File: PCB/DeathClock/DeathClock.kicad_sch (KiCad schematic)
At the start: 1 part

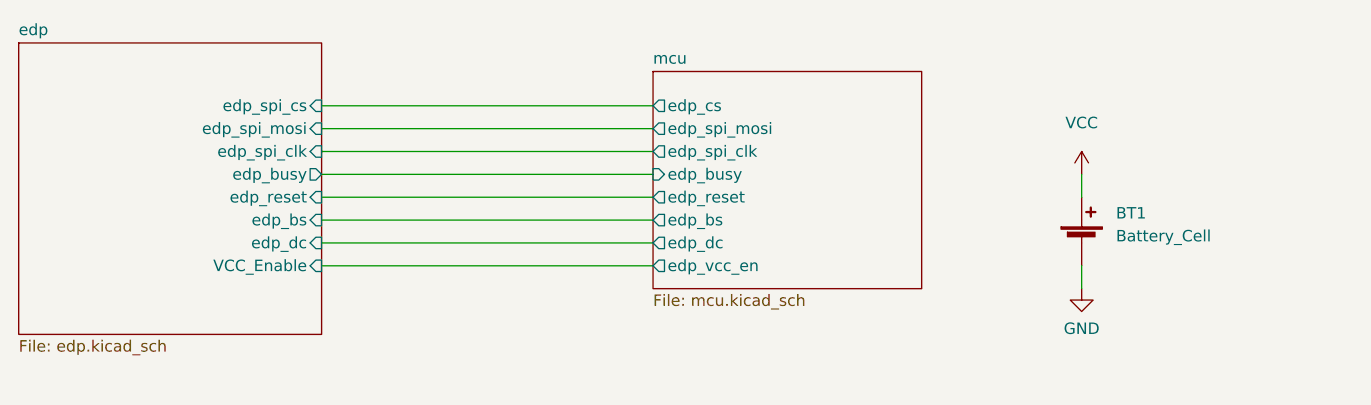
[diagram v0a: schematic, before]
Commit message: made the coin cell symbol 4 pins to make drc happy
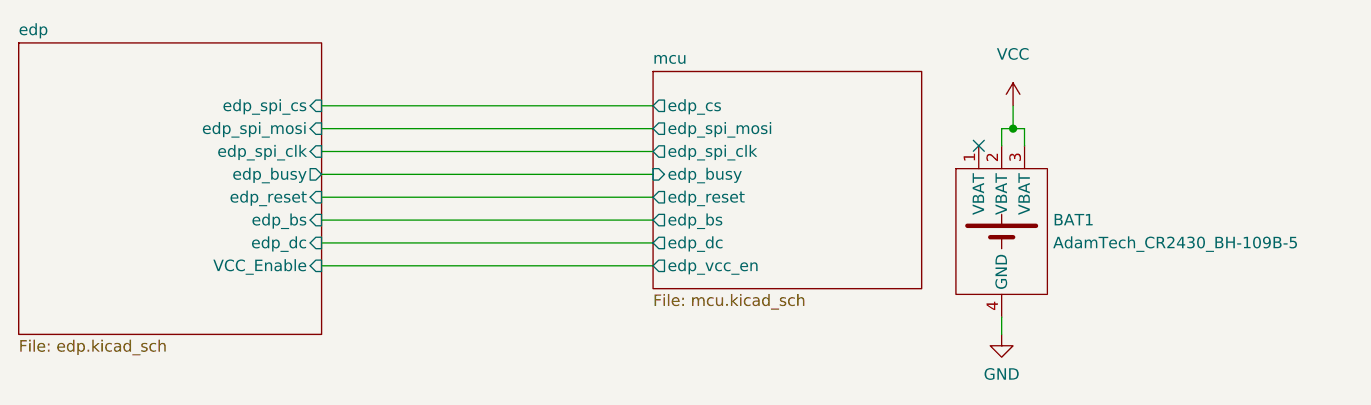
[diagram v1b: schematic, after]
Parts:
- removed BT1: Battery_Cell, CoinCellHolder:AdamTech_CR2430_BH-109B-5, symbol Device:Battery_Cell
- added BAT1: AdamTech_CR2430_BH-109B-5, CoinCellHolder:AdamTech_CR2430_BH-109B-5_num_pads, symbol CoinCellHolder:AdamTech_CR2430_BH-109B-5
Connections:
- net GND: now also BAT1.4 (GND)
- net VCC: now also BAT1.2 (VBAT), BAT1.3 (VBAT)
- no-connect marks 0 -> 1
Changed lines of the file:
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@@
 (kicad_sch (version 20211123) (generator eeschema)
   (paper "A4")
+  (junction (at 216.535 50.8) (diameter 0) (color 0 0 0 0)
+  )
+  (no_connect (at 212.725 52.705))
+  (wire (pts (xy 215.265 71.755) (xy 215.265 73.66))
+    (stroke (width 0) (type default) (color 0 0 0 0))
+  )
   (wire (pts (xy 139.7 55.88) (xy 176.53 55.88))
     (stroke (width 0) (type default) (color 0 0 0 0))
@@
     (stroke (width 0) (type default) (color 0 0 0 0))
   )
+  (wire (pts (xy 216.535 50.8) (xy 215.265 50.8))
+    (stroke (width 0) (type default) (color 0 0 0 0))
+  )
+  (wire (pts (xy 217.805 50.8) (xy 216.535 50.8))
+    (stroke (width 0) (type default) (color 0 0 0 0))
+  )
   (wire (pts (xy 139.7 58.42) (xy 176.53 58.42))
     (stroke (width 0) (type default) (color 0 0 0 0))
   )
-  (wire (pts (xy 224.155 55.88) (xy 224.155 58.42))
-    (stroke (width 0) (type default) (color 0 0 0 0))
-  )
   (wire (pts (xy 139.7 48.26) (xy 176.53 48.26))
     (stroke (width 0) (type default) (color 0 0 0 0))
   )
-  (wire (pts (xy 224.155 66.04) (xy 224.155 68.58))
+  (wire (pts (xy 216.535 48.26) (xy 216.535 50.8))
+    (stroke (width 0) (type default) (color 0 0 0 0))
+  )
+  (wire (pts (xy 215.265 50.8) (xy 215.265 52.705))
     (stroke (width 0) (type default) (color 0 0 0 0))
   )
@@
     (stroke (width 0) (type default) (color 0 0 0 0))
   )
+  (wire (pts (xy 217.805 52.705) (xy 217.805 50.8))
+    (stroke (width 0) (type default) (color 0 0 0 0))
+  )
   (wire (pts (xy 139.7 63.5) (xy 176.53 63.5))
     (stroke (width 0) (type default) (color 0 0 0 0))
   )
-  (symbol (lib_id "power:GND") (at 224.155 68.58 0) (unit 1)
+  (symbol (lib_id "power:GND") (at 215.265 73.66 0) (unit 1)
     (in_bom yes) (on_board yes) (fields_autoplaced)
-    (property "Reference" "#PWR014" (id 0) (at 224.155 74.93 0)
-      (effects (font (size 1.27 1.27)) hide)
-    )
-    (property "Value" "GND" (id 1) (at 224.155 73.025 0))
-    (property "Footprint" "" (id 2) (at 224.155 68.58 0)
-      (effects (font (size 1.27 1.27)) hide)
-    )
-    (property "Datasheet" "" (id 3) (at 224.155 68.58 0)
+    (property "Reference" "#PWR014" (id 0) (at 215.265 80.01 0)
+      (effects (font (size 1.27 1.27)) hide)
+    )
+    (property "Value" "GND" (id 1) (at 215.265 78.105 0))
+    (property "Footprint" "" (id 2) (at 215.265 73.66 0)
+      (effects (font (size 1.27 1.27)) hide)
+    )
+    (property "Datasheet" "" (id 3) (at 215.265 73.66 0)
       (effects (font (size 1.27 1.27)) hide)
     )
     (pin "1")
   )
-  (symbol (lib_id "Device:Battery_Cell") (at 224.155 63.5 0) (unit 1)
+  (symbol (lib_id "CoinCellHolder:AdamTech_CR2430_BH-109B-5") (at 219.075 37.465 0) (unit 1)
     (in_bom yes) (on_board yes) (fields_autoplaced)
-    (property "Reference" "BT1" (id 0) (at 227.965 60.1979 0)
-      (effects (font (size 1.27 1.27)) (justify left))
-    )
-    (property "Value" "Battery_Cell" (id 1) (at 227.965 62.7379 0)
-      (effects (font (size 1.27 1.27)) (justify left))
-    )
-    (property "Footprint" "CoinCellHolder:AdamTech_CR2430_BH-109B-5" (id 2) (at 224.155 61.976 90)
-      (effects (font (size 1.27 1.27)) hide)
-    )
-    (property "Datasheet" "~" (id 3) (at 224.155 61.976 90)
+    (property "Reference" "BAT1" (id 0) (at 220.98 60.9599 0)
+      (effects (font (size 1.27 1.27)) (justify left))
+    )
+    (property "Value" "AdamTech_CR2430_BH-109B-5" (id 1) (at 220.98 63.4999 0)
+      (effects (font (size 1.27 1.27)) (justify left))
+    )
+    (property "Footprint" "CoinCellHolder:AdamTech_CR2430_BH-109B-5_num_pads" (id 2) (at 219.075 37.465 0)
+      (effects (font (size 1.27 1.27)) hide)
+    )
+    (property "Datasheet" "" (id 3) (at 219.075 37.465 0)
       (effects (font (size 1.27 1.27)) hide)
     )
     (pin "1")
     (pin "2")
-  )
-  (symbol (lib_id "power:VCC") (at 224.155 55.88 0) (unit 1)
+    (pin "3")
+    (pin "4")
+  )
+  (symbol (lib_id "power:VCC") (at 216.535 48.26 0) (unit 1)
     (in_bom yes) (on_board yes) (fields_autoplaced)
-    (property "Reference" "#PWR03" (id 0) (at 224.155 59.69 0)
-      (effects (font (size 1.27 1.27)) hide)
-    )
-    (property "Value" "VCC" (id 1) (at 224.155 50.165 0))
-    (property "Footprint" "" (id 2) (at 224.155 55.88 0)
-      (effects (font (size 1.27 1.27)) hide)
-    )
-    (property "Datasheet" "" (id 3) (at 224.155 55.88 0)
+    (property "Reference" "#PWR03" (id 0) (at 216.535 52.07 0)
+      (effects (font (size 1.27 1.27)) hide)
+    )
+    (property "Value" "VCC" (id 1) (at 216.535 42.545 0))
+    (property "Footprint" "" (id 2) (at 216.535 48.26 0)
+      (effects (font (size 1.27 1.27)) hide)
+    )
+    (property "Datasheet" "" (id 3) (at 216.535 48.26 0)
       (effects (font (size 1.27 1.27)) hide)
     )
@@
       (reference "#PWR013") (unit 1) (value "GND") (footprint "")
     )
-    (path "/29052f11-eb52-41b4-aa3f-c148433f61d5"
+    (path "/db221e2e-16e2-411b-9678-0f2bcd58a060"
       (reference "#PWR014") (unit 1) (value "GND") (footprint "")
     )
@@
       (reference "#PWR0104") (unit 1) (value "VCC") (footprint "")
     )
-    (path "/626b5ec8-8450-48aa-9676-e66ed01335de"
-      (reference "BT1") (unit 1) (value "Battery_Cell") (footprint "CoinCellHolder:AdamTech_CR2430_BH-109B-5")
+    (path "/e9aeae42-e3cd-4459-8869-9c06e862b995"
+      (reference "BAT1") (unit 1) (value "AdamTech_CR2430_BH-109B-5") (footprint "CoinCellHolder:AdamTech_CR2430_BH-109B-5_num_pads")
     )
     (path "/a411903f-4de6-4ee7-aee3-770ddf1a3374/7be3599b-d07e-43e3-94e9-389e631ed847"
@@
     )
     (path "/b426553d-4a7e-4896-84cf-af69497a695e/62c8f91e-d081-45a0-b641-212a01ca41a3"
-      (reference "C11") (unit 1) (value "C") (footprint "Capacitor_SMD:C_0402_1005Metric_Pad0.74x0.62mm_HandSolder")
+      (reference "C11") (unit 1) (value "6pF") (footprint "Capacitor_SMD:C_0402_1005Metric_Pad0.74x0.62mm_HandSolder")
     )
     (path "/b426553d-4a7e-4896-84cf-af69497a695e/c2995412-0125-46b5-84e5-f87417db8fb5"
-      (reference "C12") (unit 1) (value "C") (footprint "Capacitor_SMD:C_0402_1005Metric_Pad0.74x0.62mm_HandSolder")
+      (reference "C12") (unit 1) (value "6pF") (footprint "Capacitor_SMD:C_0402_1005Metric_Pad0.74x0.62mm_HandSolder")
     )
     (path "/b426553d-4a7e-4896-84cf-af69497a695e/c7f3ff9d-d6a2-4b63-86d7-50e2b919e98f"
-      (reference "C13") (unit 1) (value "C") (footprint "Capacitor_SMD:C_0402_1005Metric_Pad0.74x0.62mm_HandSolder")
+      (reference "C13") (unit 1) (value "1uF") (footprint "Capacitor_SMD:C_0402_1005Metric_Pad0.74x0.62mm_HandSolder")
     )
     (path "/b426553d-4a7e-4896-84cf-af69497a695e/6fc5aafb-5a22-4bda-8f08-f38eb0e112cc"
-      (reference "C14") (unit 1) (value "C") (footprint "Capacitor_SMD:C_0402_1005Metric_Pad0.74x0.62mm_HandSolder")
+      (reference "C14") (unit 1) (value "0.1uF") (footprint "Capacitor_SMD:C_0402_1005Metric_Pad0.74x0.62mm_HandSolder")
     )
     (path "/b426553d-4a7e-4896-84cf-af69497a695e/5160cae1-c9cd-47c0-a486-270ddd6b1f4a"
-      (reference "C15") (unit 1) (value "C") (footprint "Capacitor_SMD:C_0402_1005Metric_Pad0.74x0.62mm_HandSolder")
+      (reference "C15") (unit 1) (value "1uF") (footprint "Capacitor_SMD:C_0402_1005Metric_Pad0.74x0.62mm_HandSolder")
     )
     (path "/b426553d-4a7e-4896-84cf-af69497a695e/deb6739a-d8ee-425e-a460-0621b78ed40d"
-      (reference "C16") (unit 1) (value "C") (footprint "Capacitor_SMD:C_0402_1005Metric_Pad0.74x0.62mm_HandSolder")
+      (reference "C16") (unit 1) (value "0.1uF") (footprint "Capacitor_SMD:C_0402_1005Metric_Pad0.74x0.62mm_HandSolder")
     )
     (path "/a411903f-4de6-4ee7-aee3-770ddf1a3374/3b188594-d8c4-4f37-9ba4-a04dccc75f15"
